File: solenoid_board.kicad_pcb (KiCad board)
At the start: 2 copper layers, 100 x 93 mm, 38 parts, among them J2 MCU_LEFT_LEGS, J3 MCU_RIGHT_LEGS

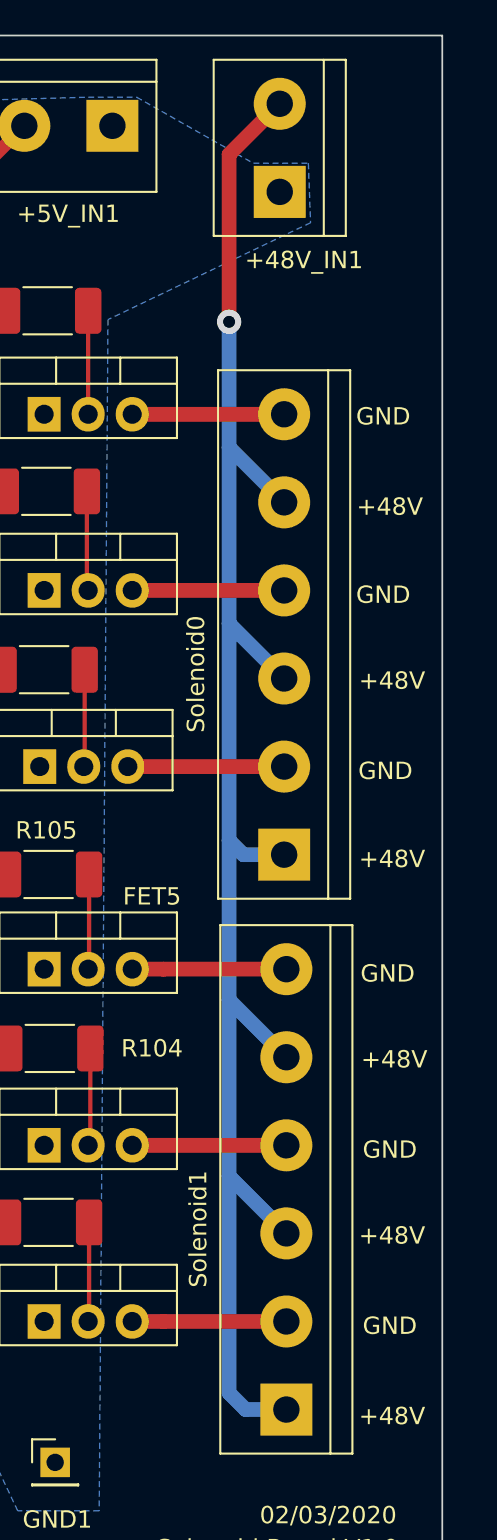
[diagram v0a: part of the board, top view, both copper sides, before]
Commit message: Increased thickness for Solenoid signal. High amperage begets a thick wire.
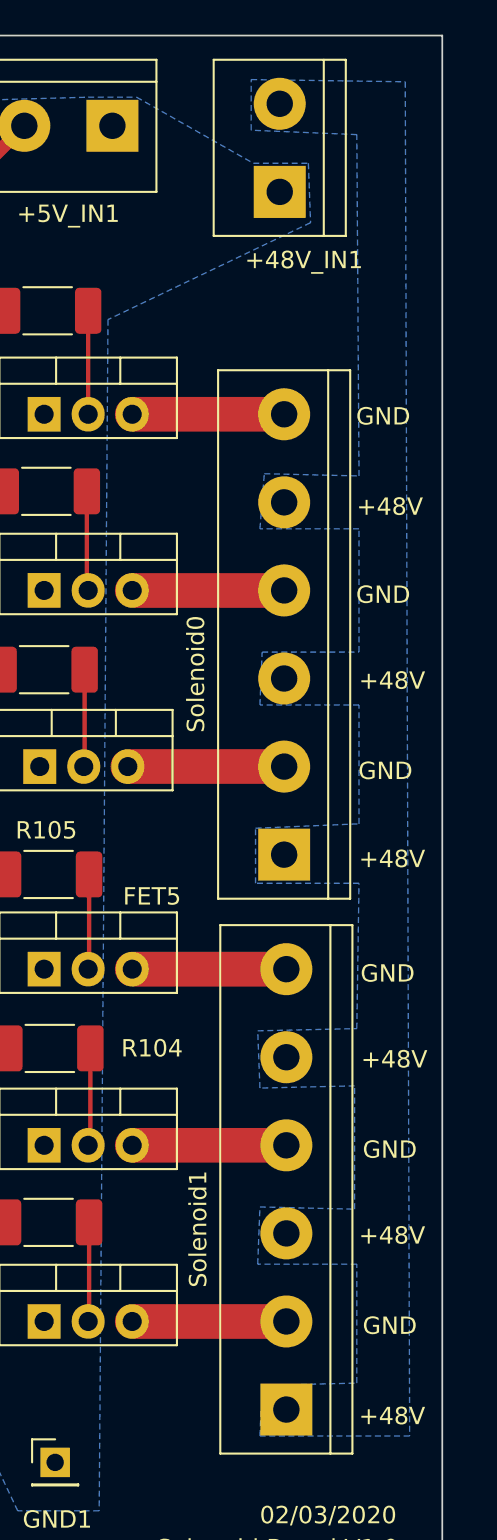
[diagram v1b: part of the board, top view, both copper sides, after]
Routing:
- net +48V: track 101.0 -> 0.00 mm, vias 1 -> 0
- added copper zone on B.Cu, net +48V

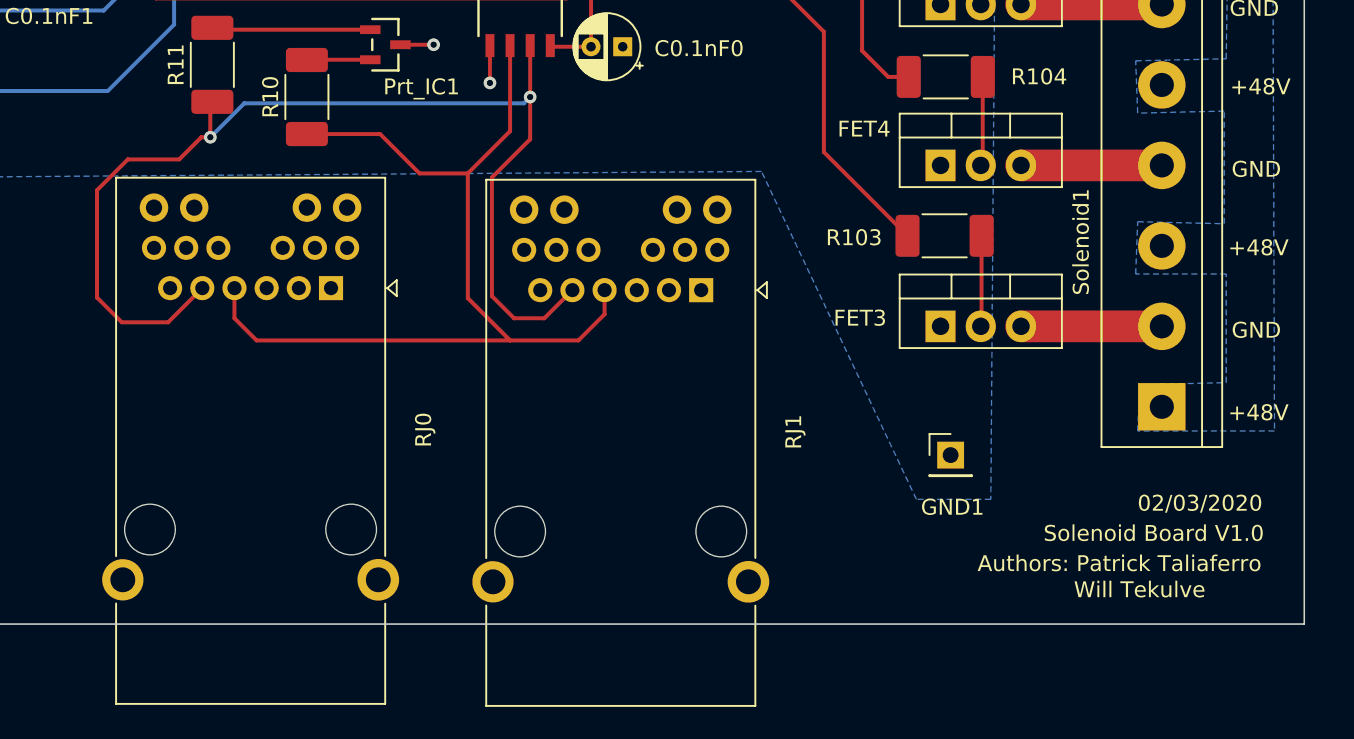
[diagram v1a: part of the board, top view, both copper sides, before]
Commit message: Swapped out RJ-45 Connectors in all documents.
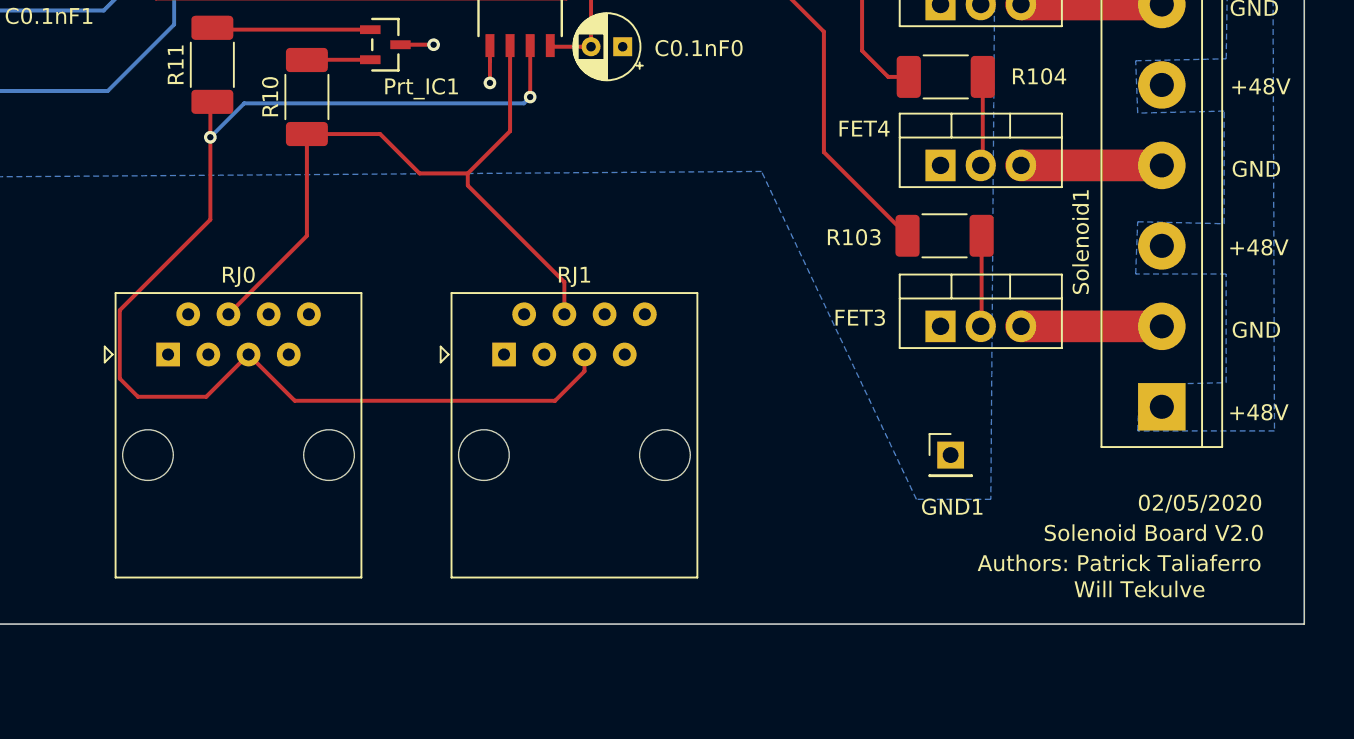
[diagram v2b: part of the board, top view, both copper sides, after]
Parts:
- RJ0, RJ1: footprint Connector_RJ:RJ45_Pulse_JK0654219NL_Horizontal -> Connector_RJ:RJ45_Amphenol_54602-x08_Horizontal
- moved RJ1 13.1 mm to (141.5, 129.3), turned to 0 degrees
- moved RJ0 11.1 mm to (120.3, 129.3), turned to 0 degrees
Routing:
- net /RJ45_4: track 60.1 -> 45.2 mm
- net /RJ45_5: track 70.2 -> 78.3 mm
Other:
- board text added: "02/05/2020"
- board text added: "Solenoid Board V2.0"
- board text removed: "02/03/2020"
- board text removed: "Solenoid Board V1.0"

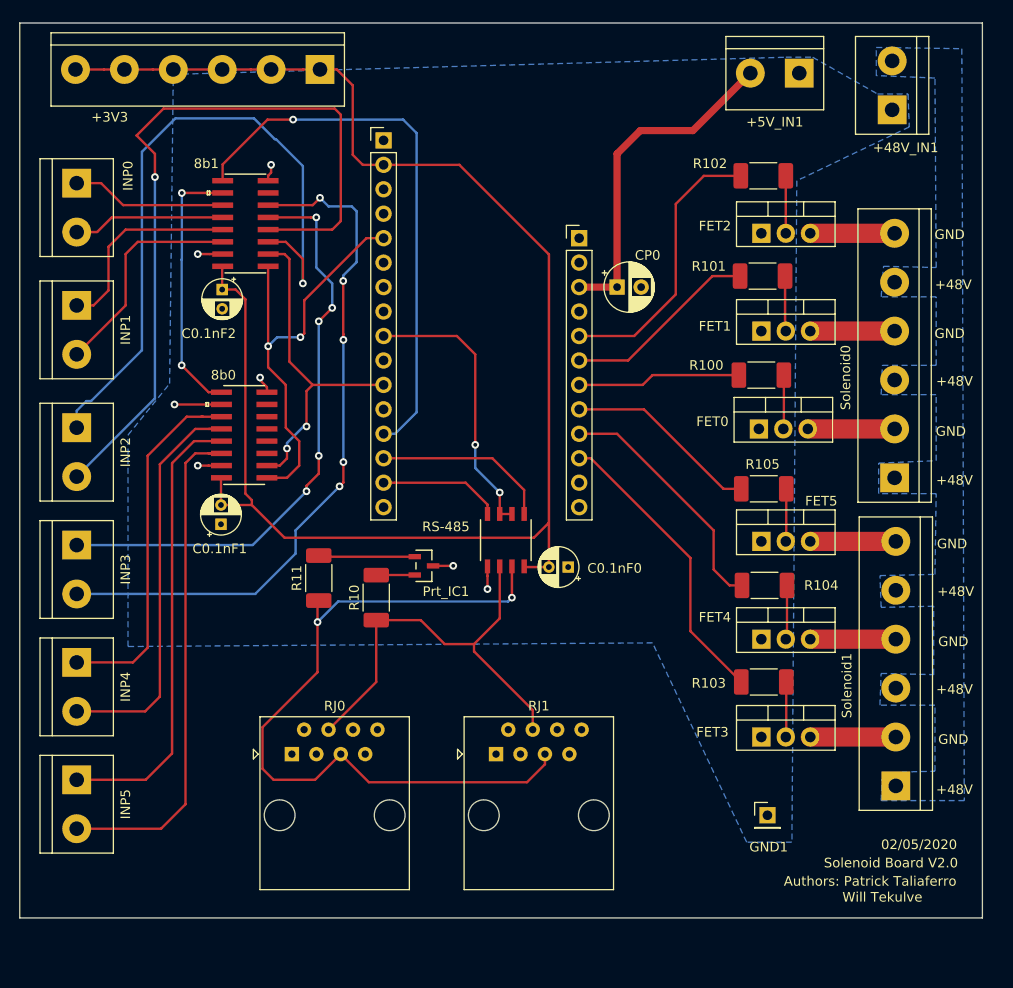
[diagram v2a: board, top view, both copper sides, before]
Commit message: Deleted all wire connections, changed board geometry, added mounting holes, specified where JLCPCB should print their Mfg. #. Next steps are to draw the new wires after we get V1 shipped in.
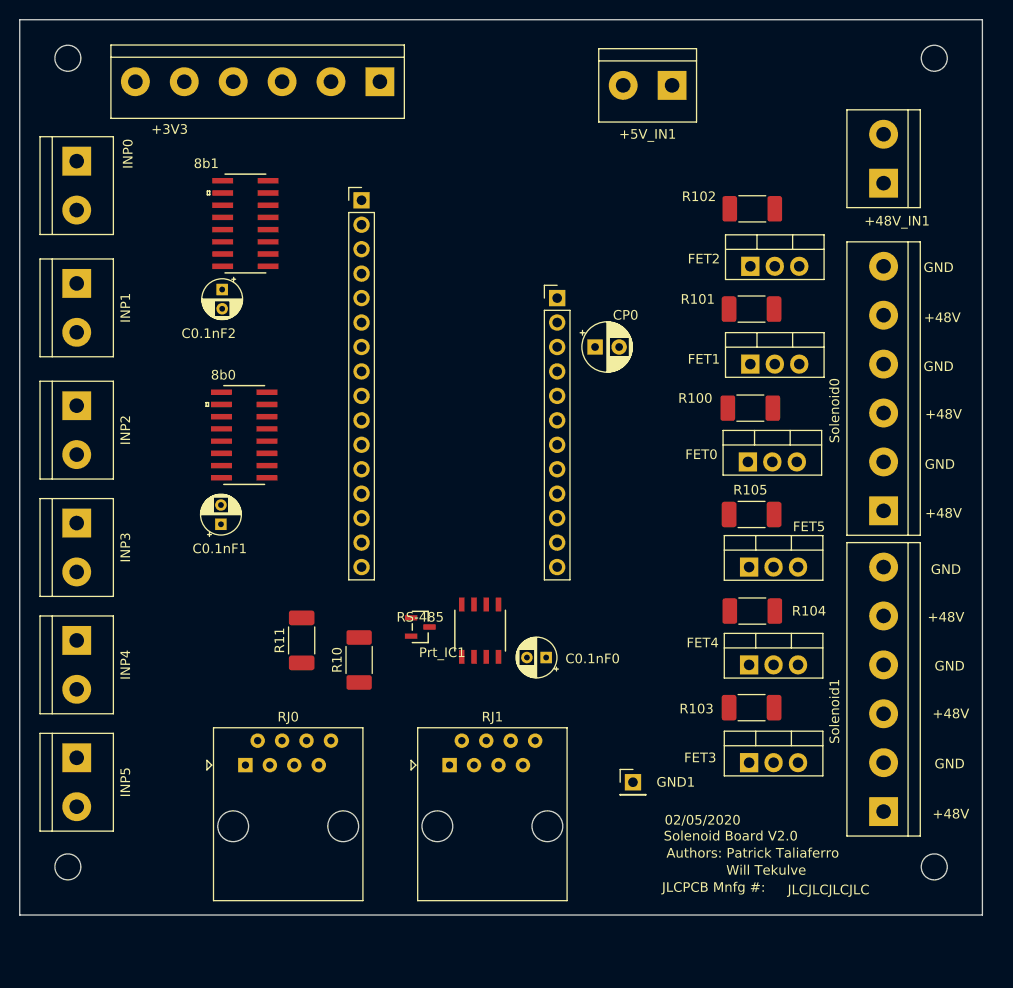
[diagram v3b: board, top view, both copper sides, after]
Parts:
- added REF**: MountingHole_2.7mm_M2.5, MountingHole:MountingHole_2.7mm_M2.5, F.Cu at (97.0, 57.0)
- added REF**: MountingHole_2.7mm_M2.5, MountingHole:MountingHole_2.7mm_M2.5, F.Cu at (187.0, 57.0)
- added REF**: MountingHole_2.7mm_M2.5, MountingHole:MountingHole_2.7mm_M2.5, F.Cu at (187.0, 141.0)
- added REF**: MountingHole_2.7mm_M2.5, MountingHole:MountingHole_2.7mm_M2.5, F.Cu at (97.0, 141.0)
- moved GND1 14.4 mm to (155.7, 132.2)
- moved +5V_IN1 13.3 mm to (159.8, 59.8)
- moved RS-485 9.77 mm to (139.8, 116.5)
- moved C0.1nF0 9.67 mm to (146.7, 119.3)
- moved +48V_IN1 7.67 mm to (181.7, 70.0)
- moved R10 6.72 mm to (127.3, 119.5)
- moved R11 6.72 mm to (121.3, 117.5)
- moved J3 6.63 mm to (147.8, 81.9)
- moved J2 6.63 mm to (127.5, 71.8)
- moved CP0 6.63 mm to (151.8, 87.0)
- moved Prt_IC1 6.36 mm to (133.6, 116.1)
- moved +3V3 6.35 mm to (129.4, 59.4)
- moved RJ1 4.96 mm to (136.7, 130.4)
- moved RJ0 4.96 mm to (115.4, 130.4)
- moved FET0 3.61 mm to (167.6, 98.9)
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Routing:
- net +3V3: track 162.3 -> 0.00 mm
- net /INP2_1: track 81.2 -> 0.00 mm, vias 1 -> 0
- net /RJ45_5: track 78.3 -> 0.00 mm, vias 2 -> 0
- net /INP3_1: track 72.8 -> 0.00 mm, vias 5 -> 0
- net /INP2_0: track 71.0 -> 0.00 mm, vias 1 -> 0
- net /INP3_0: track 61.4 -> 0.00 mm, vias 5 -> 0
- net /MISO: track 57.7 -> 0.00 mm, vias 1 -> 0
- net /INP5_1: track 53.3 -> 0.00 mm
- net /INP5_0: track 47.3 -> 0.00 mm
- net /RJ45_4: track 45.2 -> 0.00 mm
- net /A0: track 44.6 -> 0.00 mm, vias 2 -> 0
- net /INP4_1: track 42.7 -> 0.00 mm
- net /INP4_0: track 37.4 -> 0.00 mm
- net /SCK: track 35.2 -> 0.00 mm, vias 2 -> 0
- net +5V: track 35.1 -> 0.00 mm
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- removed copper zone on B.Cu, net +48V
- removed copper zone on B.Cu, net GND
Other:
- board text added: "JLCJLCJLCJLC"
- board text added: "JLCPCB Mnfg #:"

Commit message: Changed the resistor footprints, and sourced new resistors in the BOM. Need to route the wires.
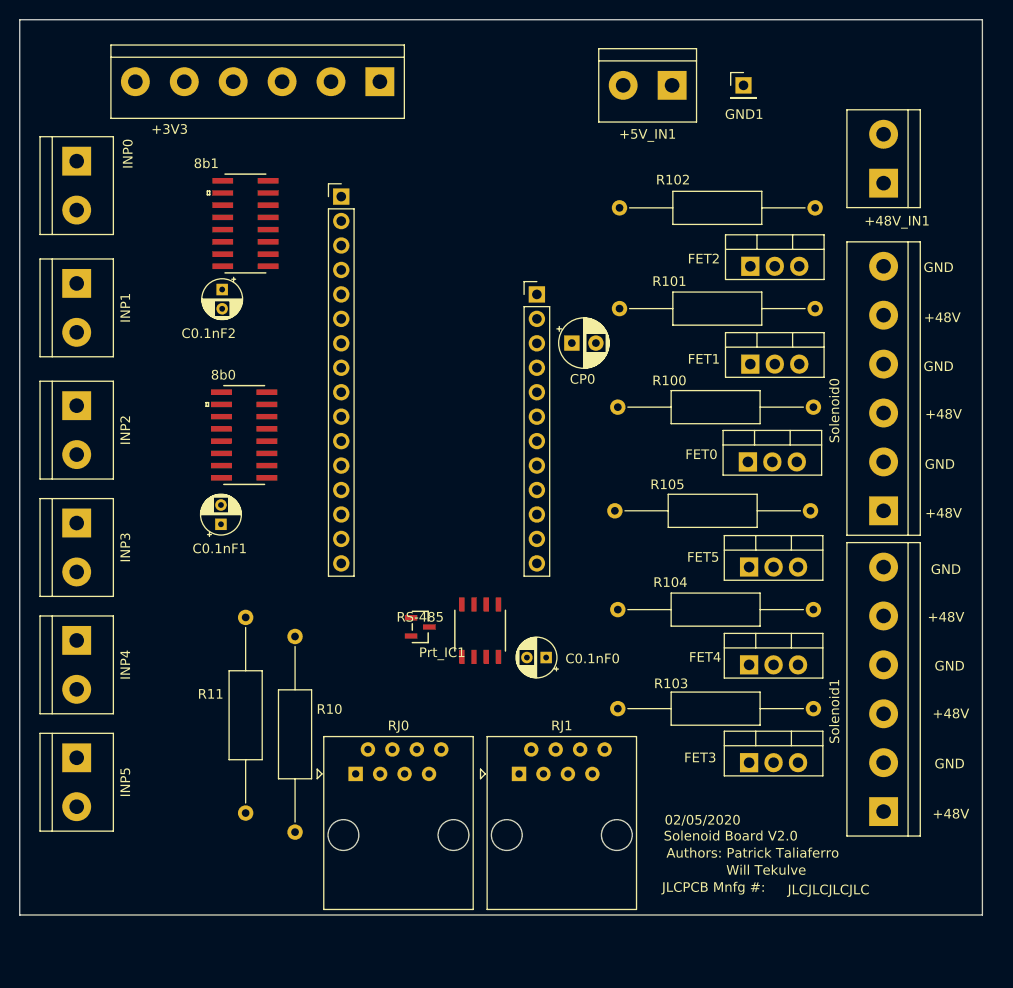
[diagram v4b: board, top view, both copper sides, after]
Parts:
- removed REF** (x4): MountingHole_2.7mm_M2.5, MountingHole:MountingHole_2.7mm_M2.5
- R10, R100, R101, R102, R103, R104, R105, R11: footprint Resistor_SMD:R_2010_5025Metric_Pad1.52x2.65mm_HandSolder -> Resistor_THT:R_Axial_DIN0309_L9.0mm_D3.2mm_P20.32mm_Horizontal
- moved GND1 73.3 mm to (167.2, 59.8)
- moved R10 19.1 mm to (120.6, 137.4)
- moved R11 18.9 mm to (115.5, 135.4)
- moved RJ0 11.5 mm to (126.9, 131.3)
- moved RJ1 7.27 mm to (143.9, 131.3)
- moved R101 6.60 mm to (174.6, 83.0)
- moved R100 6.55 mm to (174.4, 93.2)
- moved R102 6.53 mm to (174.6, 72.5)
- moved R103 6.43 mm to (174.4, 124.6)
- moved R104 6.35 mm to (174.4, 114.3)
- moved R105 6.13 mm to (174.1, 104.0)
- moved CP0 2.45 mm to (149.4, 86.6)
- moved J3 2.14 mm to (145.7, 81.5)
- moved J2 2.14 mm to (125.4, 71.4)
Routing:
- net /D12: track 0.87 -> 0.00 mm

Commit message: Finished V2 Routing.
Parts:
- moved Prt_IC1 6.88 mm to (126.7, 116.1)
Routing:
- net +3V3: track 0.00 -> 165.4 mm
- net /INP3_0: track 0.00 -> 79.9 mm, vias 0 -> 2
- net /INP3_1: track 0.00 -> 68.7 mm, vias 0 -> 2
- net /MISO: track 0.00 -> 59.4 mm, vias 0 -> 2
- net /RJ45_5: track 0.00 -> 59.0 mm
- net /INP5_1: track 0.00 -> 48.8 mm
- net GND: track 0.00 -> 47.0 mm, vias 0 -> 3
- net /RJ45_4: track 0.00 -> 46.8 mm, vias 0 -> 1
- net /INP5_0: track 0.00 -> 44.4 mm
- net /INP2_1: track 0.00 -> 41.7 mm, vias 0 -> 1
- net /INP4_1: track 0.00 -> 38.2 mm
- net /INP2_0: track 0.00 -> 35.5 mm, vias 0 -> 1
- net /SCK: track 0.00 -> 33.9 mm
- net /INP4_0: track 0.00 -> 33.5 mm
- net /A0: track 0.00 -> 33.3 mm, vias 0 -> 2
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- added copper zone on B.Cu, net +48V
- added copper zone on B.Cu, net GND
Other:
- board text added: "+5V"
